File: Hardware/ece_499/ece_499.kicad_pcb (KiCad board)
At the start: 2 copper layers, 110.8 x 70 mm, 60 parts, among them J1 Conn_01x04, J2 Conn_01x04, J3 Conn_01x04, J4 Conn_01x04, J5 Conn_01x04, Q1 DMN2004WK, Q2 DMN2004WK, Q3 DMN2004WK, Q4 DMN2004WK, SW1 Encoder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

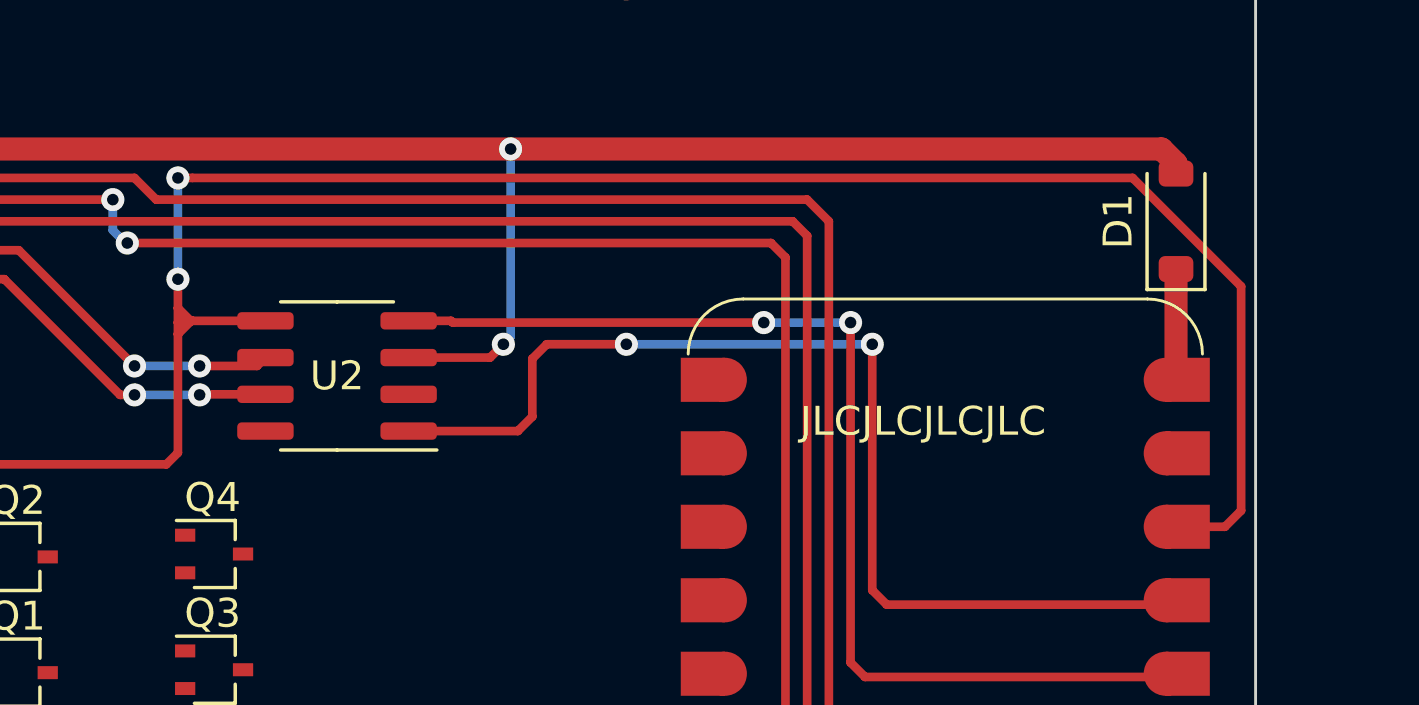
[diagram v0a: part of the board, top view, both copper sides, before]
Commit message: clean up 3v3 trace
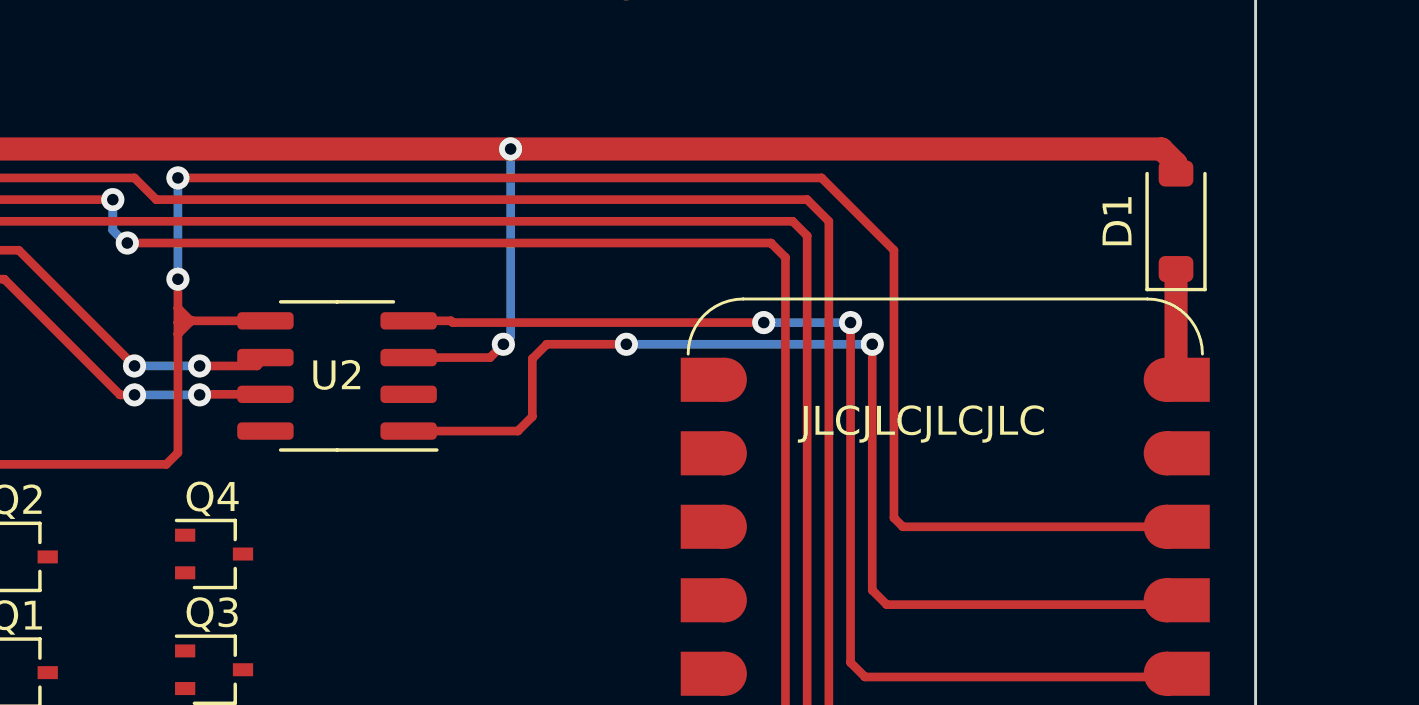
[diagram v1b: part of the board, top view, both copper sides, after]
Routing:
- net +3V3: track 113.8 -> 111.0 mm
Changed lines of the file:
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@@
 	)
 	(segment
-		(start 206.5 52)
-		(end 174 52)
-		(width 0.3)
-		(layer "F.Cu")
-		(net 27)
-	)
-	(segment
-		(start 174 52)
-		(end 173.5 52)
+		(start 198.25 54.5)
+		(end 195.75 52)
 		(width 0.3)
 		(layer "F.Cu")
@@
 		(start 161.65 61.9)
 		(end 162 62.25)
-		(width 0.3)
-		(layer "F.Cu")
-		(net 27)
-	)
-	(segment
-		(start 208.407 64.0585)
-		(end 209.6915 64.0585)
-		(width 0.3)
-		(layer "F.Cu")
-		(net 27)
-	)
-	(segment
-		(start 210.25 63.5)
-		(end 210.25 55.75)
 		(width 0.3)
 		(layer "F.Cu")
@@
 		(start 162.5 61.9)
 		(end 162.35 61.9)
+		(width 0.3)
+		(layer "F.Cu")
+		(net 27)
+	)
+	(segment
+		(start 195.75 52)
+		(end 173.5 52)
 		(width 0.3)
 		(layer "F.Cu")
@@
 	)
 	(segment
-		(start 210.25 55.75)
-		(end 206.5 52)
+		(start 173.5 61.5)
+		(end 173.5 57.4)
 		(width 0.3)
 		(layer "F.Cu")
@@
 	)
 	(segment
-		(start 173.5 61.5)
-		(end 173.5 57.4)
+		(start 198.5585 64.0585)
+		(end 198.25 63.75)
+		(width 0.3)
+		(layer "F.Cu")
+		(net 27)
+	)
+	(segment
+		(start 208.407 64.0585)
+		(end 198.5585 64.0585)
 		(width 0.3)
 		(layer "F.Cu")
@@
 	)
 	(segment
-		(start 173.96 56.94)
-		(end 173.5 57.4)
+		(start 198.25 63.75)
+		(end 198.25 54.5)
 		(width 0.3)
 		(layer "F.Cu")
@@
 	)
 	(segment
-		(start 209.6915 64.0585)
-		(end 210.25 63.5)
+		(start 173.96 56.94)
+		(end 173.5 57.4)
 		(width 0.3)
 		(layer "F.Cu")

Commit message: Initial valve FET connections
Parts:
- moved Q1 4.10 mm to (168.0, 65.0)
- moved Q2 4.00 mm to (168.0, 69.1)
- moved Q3 4.00 mm to (174.8, 65.0)
- moved Q4 4.00 mm to (174.8, 69.0)
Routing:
- net +12V: track 296.7 -> 356.4 mm, vias 1 -> 4
- net valve_2: track 0.00 -> 30.9 mm, vias 0 -> 2
- net valve_1: track 0.00 -> 30.8 mm, vias 0 -> 2
- net valve_3: track 0.00 -> 25.1 mm, vias 0 -> 2
- net valve_4: track 0.00 -> 24.4 mm, vias 0 -> 2
- net Net-(J1-Pin_2): track 0.00 -> 10.8 mm
- net Net-(J3-Pin_2): track 0.00 -> 9.87 mm
- net Net-(J2-Pin_2): track 0.00 -> 5.81 mm
- net Net-(J4-Pin_2): track 0.00 -> 5.64 mm

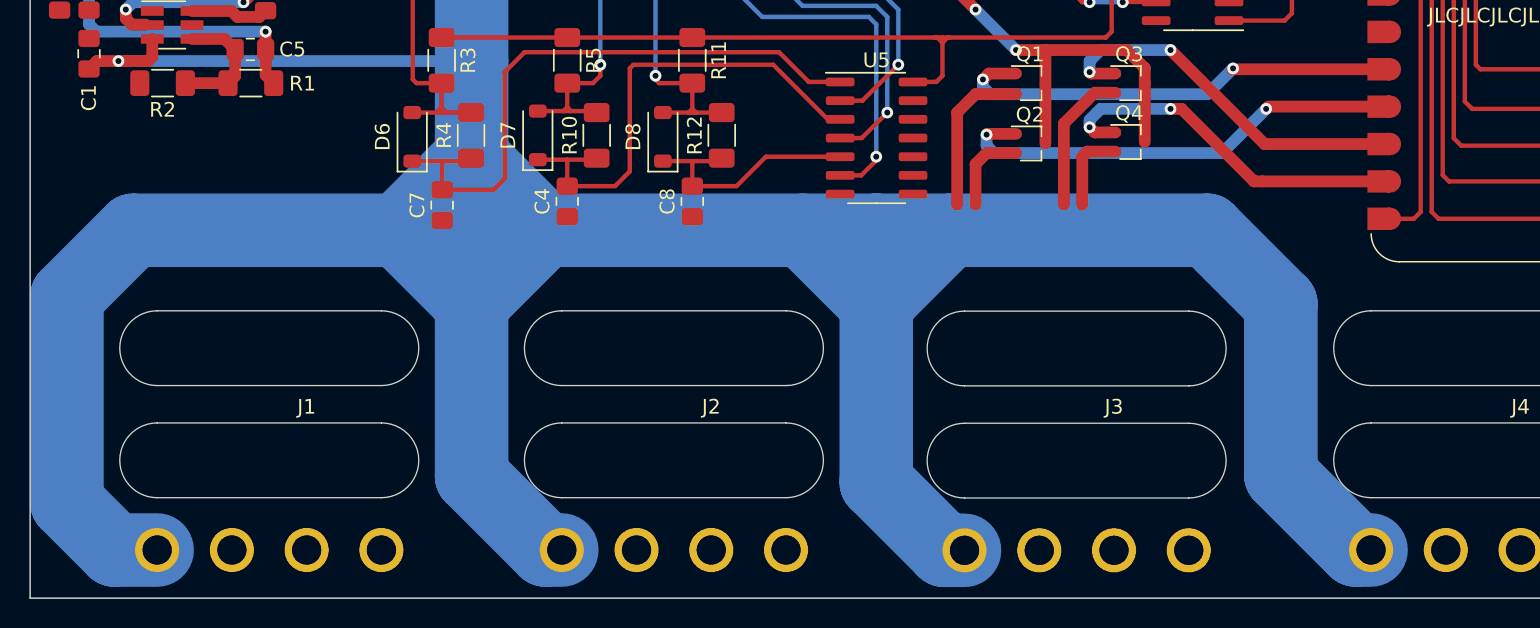
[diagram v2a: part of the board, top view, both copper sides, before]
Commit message: More valve FET -> connector
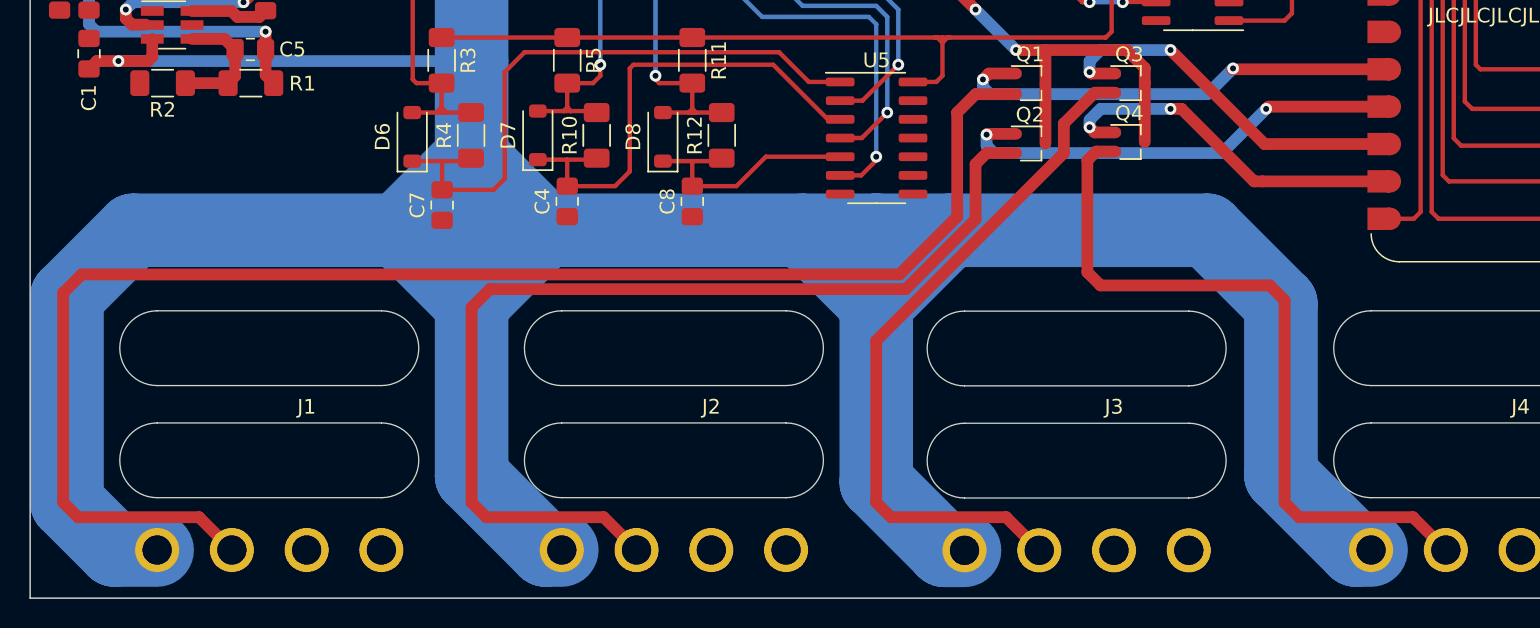
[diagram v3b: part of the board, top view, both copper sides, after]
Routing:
- net Net-(J1-Pin_2): track 10.8 -> 101.5 mm
- net Net-(J2-Pin_2): track 5.81 -> 69.3 mm
- net Net-(J4-Pin_2): track 5.64 -> 50.0 mm
- net Net-(J3-Pin_2): track 9.87 -> 47.8 mm
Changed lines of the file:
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@@
 	)
 	(segment
-		(start 167 65.75)
+		(start 103.25 94.5)
+		(end 102.25 93.5)
+		(width 0.8)
+		(layer "F.Cu")
+		(net 16)
+	)
+	(segment
+		(start 102.25 93.5)
+		(end 102.25 79.25)
+		(width 0.8)
+		(layer "F.Cu")
+		(net 16)
+	)
+	(segment
+		(start 163 67)
 		(end 164.25 65.75)
 		(width 0.8)
@@
 	(segment
 		(start 164.25 65.75)
+		(end 167 65.75)
+		(width 0.8)
+		(layer "F.Cu")
+		(net 16)
+	)
+	(segment
+		(start 113.71 96.7295)
+		(end 111.4805 94.5)
+		(width 0.8)
+		(layer "F.Cu")
+		(net 16)
+	)
+	(segment
+		(start 111.4805 94.5)
+		(end 103.25 94.5)
+		(width 0.8)
+		(layer "F.Cu")
+		(net 16)
+	)
+	(segment
+		(start 103.5 78)
+		(end 159.085786 78)
+		(width 0.8)
+		(layer "F.Cu")
+		(net 16)
+	)
+	(segment
+		(start 102.25 79.25)
+		(end 103.5 78)
+		(width 0.8)
+		(layer "F.Cu")
+		(net 16)
+	)
+	(segment
+		(start 163 74.085786)
 		(end 163 67)
 		(width 0.8)
@@
 	)
 	(segment
-		(start 163 67)
-		(end 163 73.25)
-		(width 0.8)
-		(layer "F.Cu")
-		(net 16)
+		(start 159.085786 78)
+		(end 163 74.085786)
+		(width 0.8)
+		(layer "F.Cu")
+		(net 16)
+	)
+	(segment
+		(start 131.25 79)
+		(end 159.5 79)
+		(width 0.8)
+		(layer "F.Cu")
+		(net 18)
+	)
+	(segment
+		(start 138.9805 94.5)
+		(end 131 94.5)
+		(width 0.8)
+		(layer "F.Cu")
+		(net 18)
+	)
+	(segment
+		(start 131 94.5)
+		(end 130 93.5)
+		(width 0.8)
+		(layer "F.Cu")
+		(net 18)
+	)
+	(segment
+		(start 130 80.25)
+		(end 131.25 79)
+		(width 0.8)
+		(layer "F.Cu")
+		(net 18)
+	)
+	(segment
+		(start 141.21 96.7295)
+		(end 138.9805 94.5)
+		(width 0.8)
+		(layer "F.Cu")
+		(net 18)
+	)
+	(segment
+		(start 165 69.75)
+		(end 167 69.75)
+		(width 0.8)
+		(layer "F.Cu")
+		(net 18)
+	)
+	(segment
+		(start 130 93.5)
+		(end 130 80.25)
+		(width 0.8)
+		(layer "F.Cu")
+		(net 18)
+	)
+	(segment
+		(start 159.5 79)
+		(end 164.25 74.25)
+		(width 0.8)
+		(layer "F.Cu")
+		(net 18)
+	)
+	(segment
+		(start 164.25 74.25)
+		(end 164.25 70.5)
+		(width 0.8)
+		(layer "F.Cu")
+		(net 18)
 	)
 	(segment
 		(start 164.25 70.5)
-		(end 164.25 73.25)
-		(width 0.8)
-		(layer "F.Cu")
-		(net 18)
-	)
-	(segment
-		(start 167 69.75)
 		(end 165 69.75)
 		(width 0.8)
@@
 	)
 	(segment
-		(start 165 69.75)
-		(end 164.25 70.5)
-		(width 0.8)
-		(layer "F.Cu")
-		(net 18)
-	)
-	(segment
-		(start 170.25 67.75)
-		(end 170.25 73.25)
+		(start 158.5 94.5)
+		(end 166.33 94.5)
+		(width 0.8)
+		(layer "F.Cu")
+		(net 20)
+	)
+	(segment
+		(start 166.33 94.5)
+		(end 168.58 96.75)
+		(width 0.8)
+		(layer "F.Cu")
+		(net 20)
+	)
+	(segment
+		(start 157.5 93.5)
+		(end 158.5 94.5)
 		(width 0.8)
 		(layer "F.Cu")
@@
 	)
 	(segment
+		(start 170.25 67.75)
+		(end 170.25 69.75)
+		(width 0.8)
+		(layer "F.Cu")
+		(net 20)
+	)
+	(segment
 		(start 173.75 65.65)
 		(end 172.35 65.65)
@@
 	)
 	(segment
-		(start 171.85 69.65)
-		(end 171.5 70)
+		(start 170.25 69.75)
+		(end 157.5 82.5)
+		(width 0.8)
+		(layer "F.Cu")
+		(net 20)
+	)
+	(segment
+		(start 157.5 82.5)
+		(end 157.5 93.5)
+		(width 0.8)
+		(layer "F.Cu")
+		(net 20)
+	)
+	(segment
+		(start 172.45 69.65)
+		(end 171.85 70.25)
+		(width 0.8)
+		(layer "F.Cu")
+		(net 22)
+	)
+	(segment
+		(start 171.85 70.25)
+		(end 171.85 77.85)
+		(width 0.8)
+		(layer "F.Cu")
+		(net 22)
+	)
+	(segment
+		(start 185.25 93.5)
+		(end 186.25 94.5)
+		(width 0.8)
+		(layer "F.Cu")
+		(net 22)
+	)
+	(segment
+		(start 172.75 78.75)
+		(end 184.25 78.75)
+		(width 0.8)
+		(layer "F.Cu")
+		(net 22)
+	)
+	(segment
+		(start 185.25 79.75)
+		(end 185.25 93.5)
 		(width 0.8)
 		(layer "F.Cu")
@@
 	(segment
 		(start 173.75 69.65)
-		(end 171.85 69.65)
-		(width 0.8)
-		(layer "F.Cu")
-		(net 22)
-	)
-	(segment
-		(start 171.5 70)
-		(end 171.5 73.25)
-		(width 0.8)
-		(layer "F.Cu")
+		(end 172.45 69.65)
+		(width 0.8)
+		(layer "F.Cu")
+		(net 22)
+	)
+	(segment
+		(start 171.85 77.85)
+		(end 172.75 78.75)
+		(width 0.8)
+		(layer "F.Cu")
+		(net 22)
+	)
+	(segment
+		(start 186.25 94.5)
+		(end 193.9805 94.5)
+		(width 0.8)
+		(layer "F.Cu")
+		(net 22)
+	)
+	(segment
+		(start 184.25 78.75)
+		(end 185.25 79.75)
+		(width 0.8)
+		(layer "F.Cu")
+		(net 22)
+	)
+	(segment
+		(start 193.9805 94.5)
+		(end 196.21 96.7295)
+		(width 0.8)
+		(layer "F.Cu")

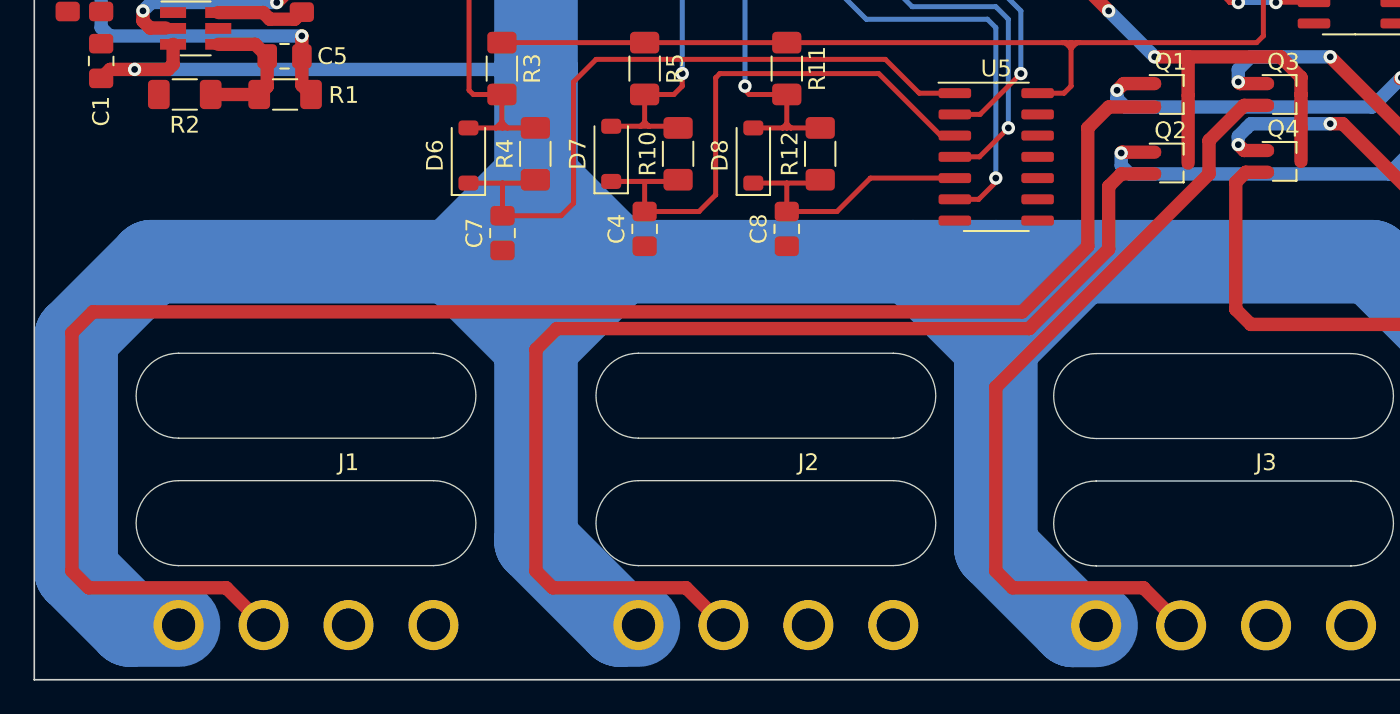
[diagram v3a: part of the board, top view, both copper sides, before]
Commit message: Add pulldowns to PCB
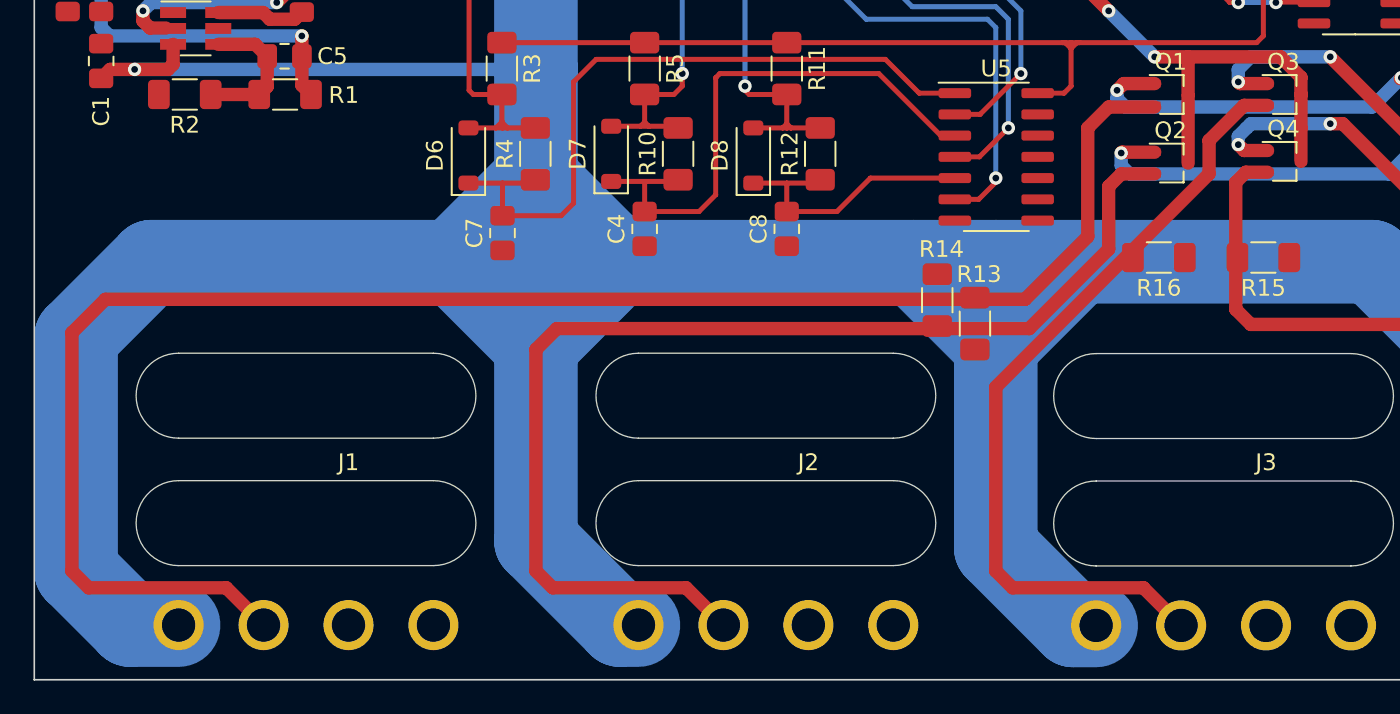
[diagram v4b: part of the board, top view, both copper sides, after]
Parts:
- added R13: 2.7k, Resistor_SMD:R_1206_3216Metric_Pad1.30x1.75mm_HandSolder, F.Cu at (156.2, 78.7)
- added R14: 2.7k, Resistor_SMD:R_1206_3216Metric_Pad1.30x1.75mm_HandSolder, F.Cu at (154.0, 77.3)
- added R15: 2.7k, Resistor_SMD:R_1206_3216Metric_Pad1.30x1.75mm_HandSolder, F.Cu at (173.5, 74.8)
- added R16: 2.7k, Resistor_SMD:R_1206_3216Metric_Pad1.30x1.75mm_HandSolder, F.Cu at (167.2, 74.8)
